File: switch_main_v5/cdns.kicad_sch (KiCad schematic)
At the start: 0 parts

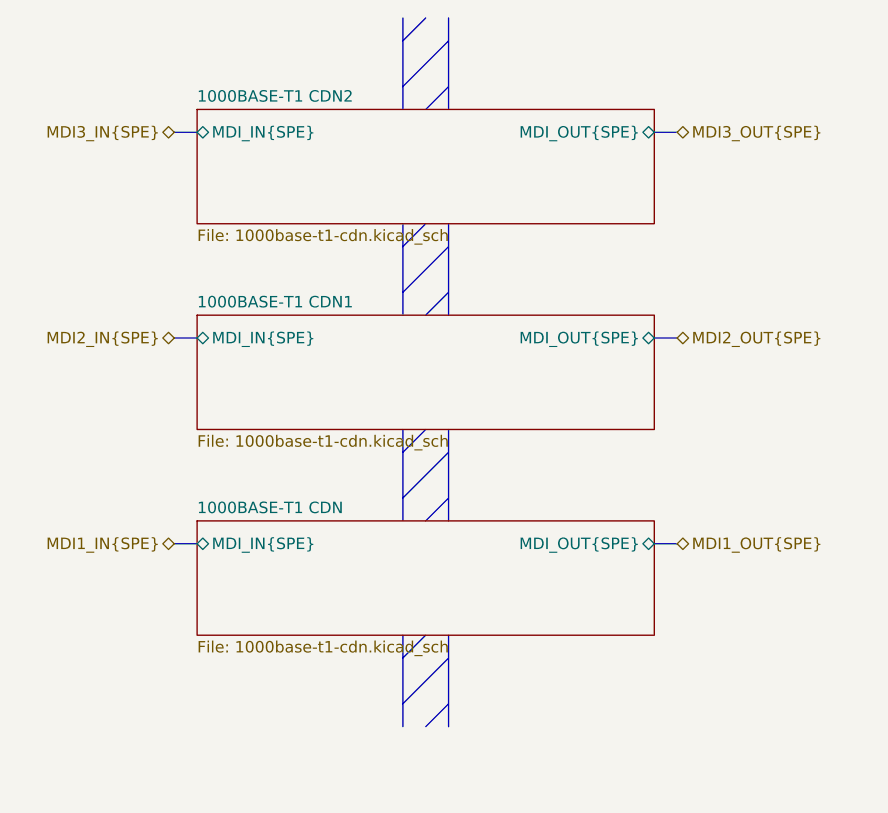
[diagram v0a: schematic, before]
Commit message: Changed main 3V3 regulator to 3A, added switch 2 crystal & other changes
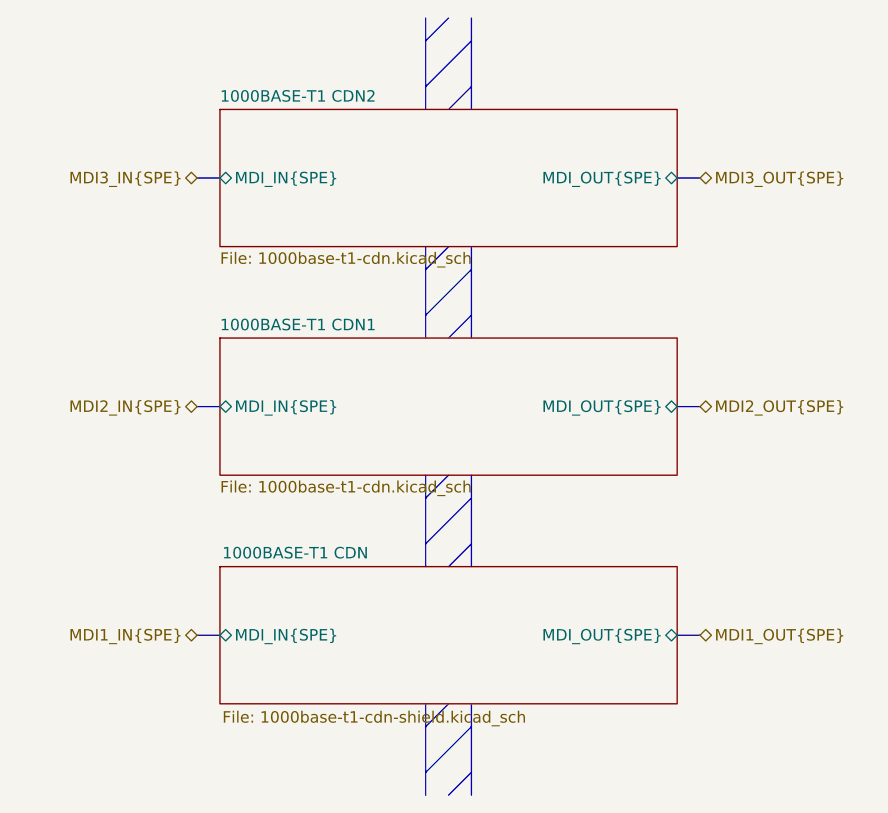
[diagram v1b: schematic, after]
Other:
- sheet 1000BASE-T1 CDN: file 1000base-t1-cdn.kicad_sch -> 1000base-t1-cdn-shield.kicad_sch

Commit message: Placed 1000BASE-T PHY decoupling capacitors
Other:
- sheet 1000BASE-T1 CDN renamed 1000BASE-T1 CDN 1
- sheet 1000BASE-T1 CDN1 renamed 1000BASE-T1 CDN 2
- sheet 1000BASE-T1 CDN2 renamed 1000BASE-T1 CDN 3
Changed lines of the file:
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@@
 			(color 248 206 204 1.0000)
 		)
-		(property "Sheetname" "1000BASE-T1 CDN"
+		(property "Sheetname" "1000BASE-T1 CDN 1"
 			(at 127.254 118.618 0)
 			(effects
@@
 			(color 248 206 204 1.0000)
 		)
-		(property "Sheetname" "1000BASE-T1 CDN2"
+		(property "Sheetname" "1000BASE-T1 CDN 3"
 			(at 127 67.8684 0)
 			(effects
@@
 			(color 248 206 204 1.0000)
 		)
-		(property "Sheetname" "1000BASE-T1 CDN1"
+		(property "Sheetname" "1000BASE-T1 CDN 2"
 			(at 127 93.2684 0)
 			(effects
